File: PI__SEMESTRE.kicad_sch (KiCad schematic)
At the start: 36 parts, among them IC1 LMV358IDR, J1 CX90B-16P1, U1 AMS1117, U11 ESP32-S3-WROOM-1, U14 BME688, U9 GUVA-S12SD

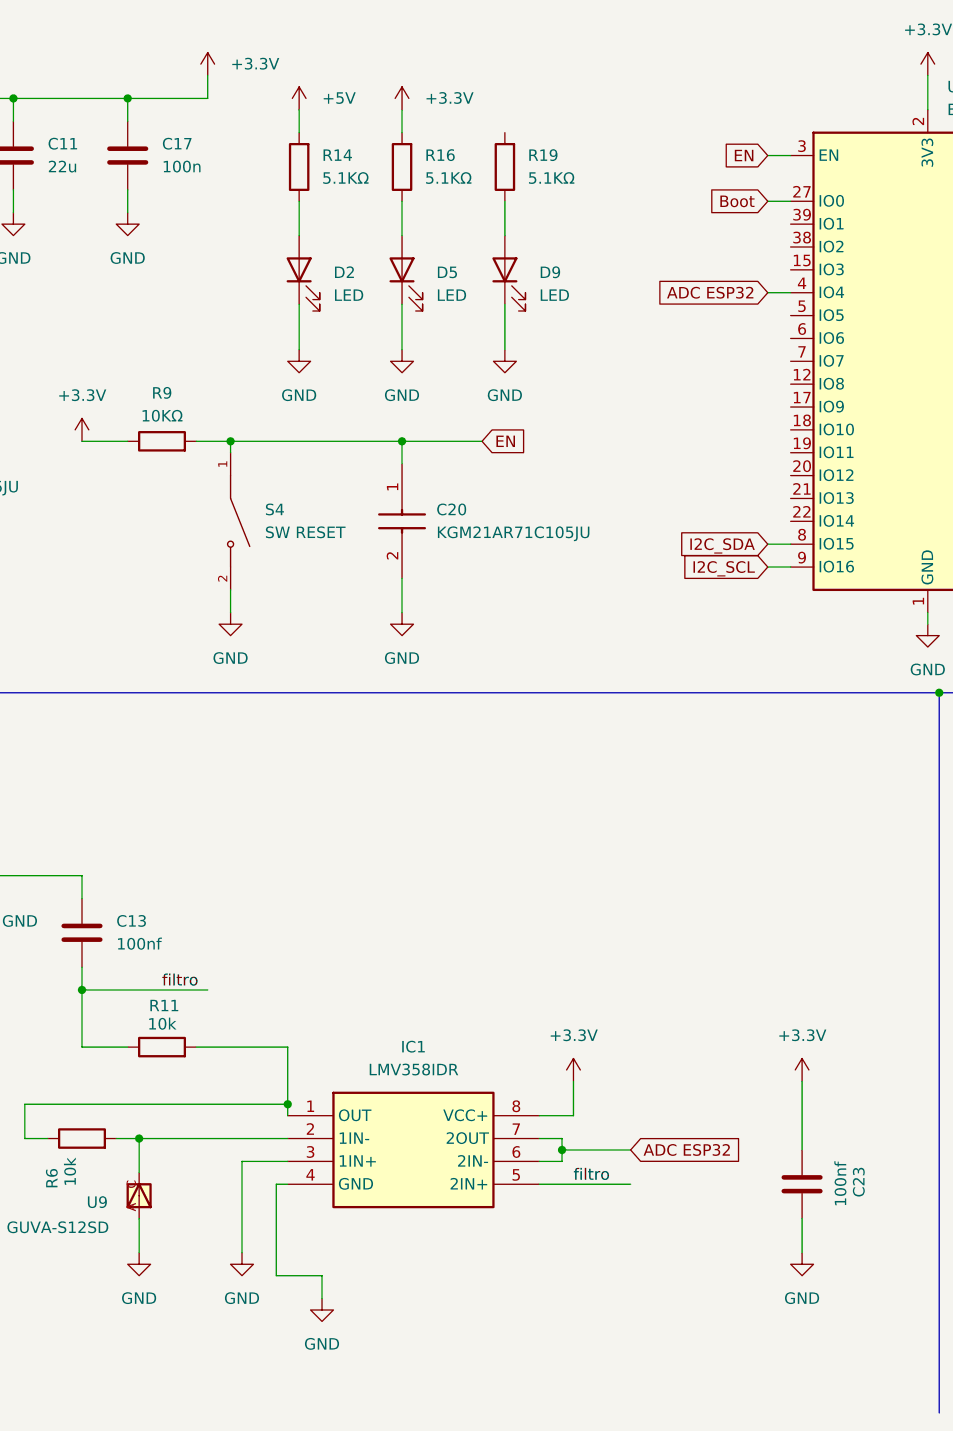
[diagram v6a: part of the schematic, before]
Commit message: se hacen los cambios de las pistas esquineras de (90 Grados) a curvas de (45 Grados) estos cambios solamente se le hicieron a las pistas azules, se le agrega la conexion del led faltante del (ESP) para nuestro KEEP ALIVE, se hace la conexion a algunas pistas faltantes que no se veian que habian por conectar, correciones de algunos GND sin conexion.
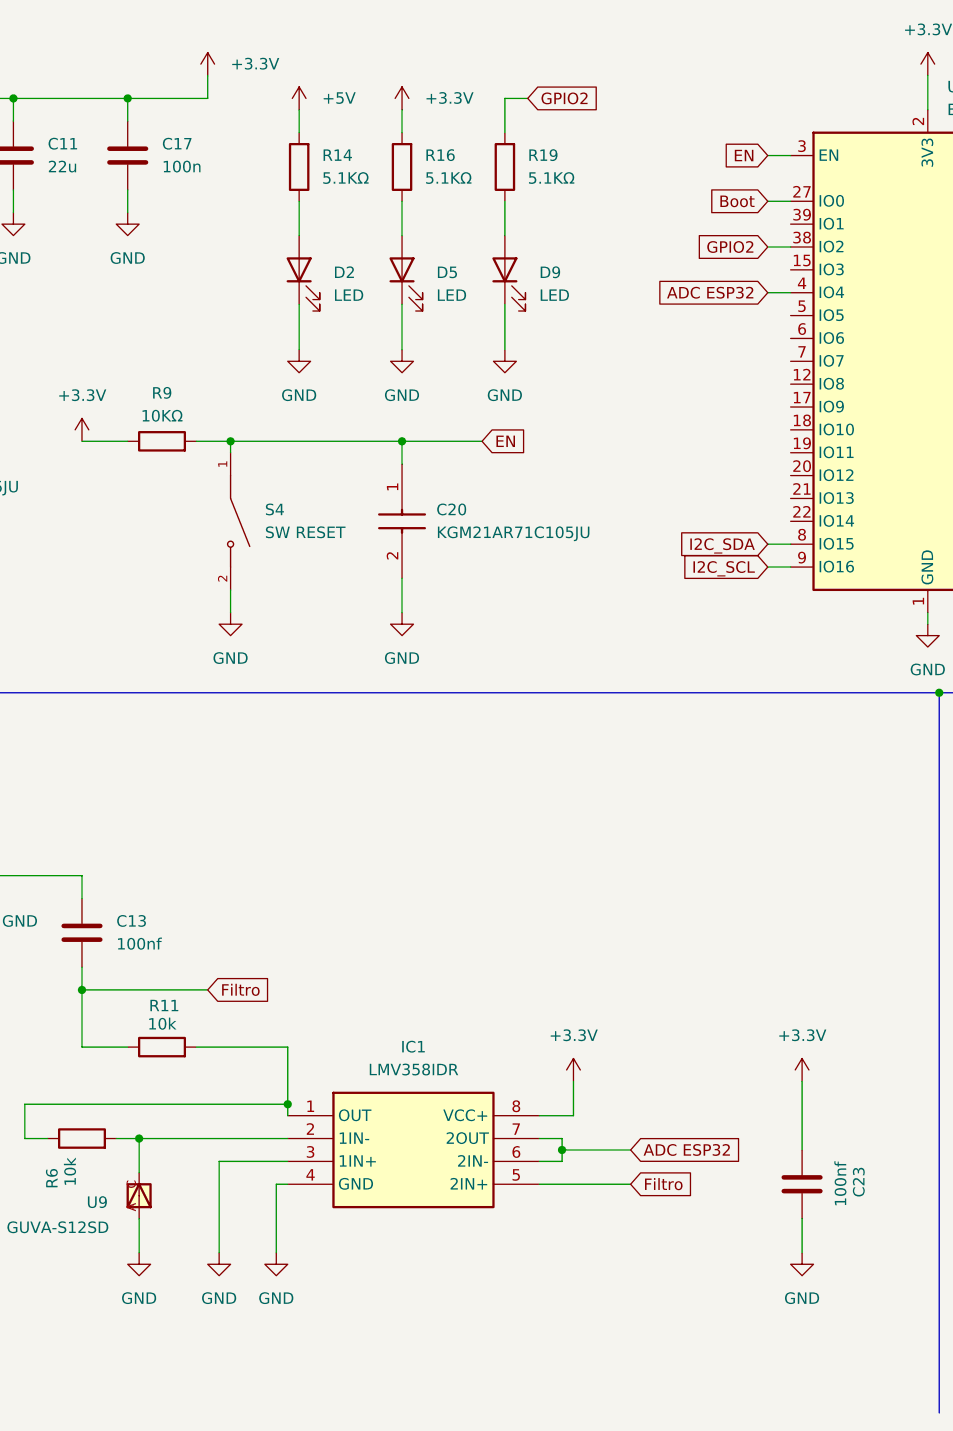
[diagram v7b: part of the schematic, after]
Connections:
- net GPIO2: now reaches R19.2
- net GPIO2: now also U11.38 (IO2)
- net filtro renamed Filtro
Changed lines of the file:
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@@
 	(wire
 		(pts
-			(xy 107.95 152.4) (xy 102.87 152.4)
-		)
-		(stroke
-			(width 0)
-			(type default)
-		)
-	)
-	(wire
-		(pts
 			(xy 232.41 130.81) (xy 234.95 130.81)
 		)
@@
 	(wire
 		(pts
-			(xy 99.06 139.7) (xy 99.06 149.86)
+			(xy 96.52 139.7) (xy 96.52 149.86)
 		)
 		(stroke
@@
 	(wire
 		(pts
+			(xy 128.27 21.59) (xy 130.81 21.59)
+		)
+		(stroke
+			(width 0)
+			(type default)
+		)
+	)
+	(wire
+		(pts
 			(xy 269.24 139.7) (xy 269.24 143.51)
 		)
@@
 	(wire
 		(pts
-			(xy 107.95 152.4) (xy 107.95 154.94)
+			(xy 73.66 24.13) (xy 73.66 21.59)
 		)
 		(stroke
@@
 	(wire
 		(pts
-			(xy 73.66 24.13) (xy 73.66 21.59)
+			(xy 224.79 33.02) (xy 224.79 35.56)
 		)
 		(stroke
@@
 	(wire
 		(pts
-			(xy 224.79 33.02) (xy 224.79 35.56)
+			(xy 128.27 25.4) (xy 128.27 21.59)
 		)
 		(stroke
@@
 	(wire
 		(pts
-			(xy 102.87 142.24) (xy 102.87 152.4)
+			(xy 102.87 142.24) (xy 102.87 149.86)
 		)
 		(stroke
@@
 	(wire
 		(pts
-			(xy 99.06 139.7) (xy 104.14 139.7)
+			(xy 96.52 139.7) (xy 104.14 139.7)
 		)
 		(stroke
@@
 	(wire
 		(pts
+			(xy 157.48 38.1) (xy 160.02 38.1)
+		)
+		(stroke
+			(width 0)
+			(type default)
+		)
+	)
+	(wire
+		(pts
 			(xy 93.98 127) (xy 104.14 127)
 		)
@@
 		)
 	)
-	(label "filtro"
-		(at 135.89 142.24 0)
-		(effects
-			(font
-				(size 1.27 1.27)
-			)
-			(justify left bottom)
-		)
-	)
-	(label "filtro"
-		(at 90.17 120.65 0)
-		(effects
-			(font
-				(size 1.27 1.27)
-			)
-			(justify left bottom)
-		)
-	)
 	(label "BME688"
 		(at 180.34 95.25 0)
@@
 		)
 	)
+	(global_label "Filtro"
+		(shape input)
+		(at 142.24 142.24 0)
+		(fields_autoplaced yes)
+		(effects
+			(font
+				(size 1.27 1.27)
+			)
+			(justify left)
+		)
+		(property "Intersheetrefs" "${INTERSHEET_REFS}"
+			(at 150.2447 142.24 0)
+			(hide yes)
+			(show_name no)
+			(do_not_autoplace no)
+			(effects
+				(font
+					(size 1.27 1.27)
+				)
+				(justify left)
+			)
+		)
+	)
 	(global_label "Boot"
 		(shape input)
@@
 		)
 	)
+	(global_label "Filtro"
+		(shape input)
+		(at 95.25 120.65 0)
+		(fields_autoplaced yes)
+		(effects
+			(font
+				(size 1.27 1.27)
+			)
+			(justify left)
+		)
+		(property "Intersheetrefs" "${INTERSHEET_REFS}"
+			(at 103.2547 120.65 0)
+			(hide yes)
+			(show_name no)
+			(do_not_autoplace no)
+			(effects
+				(font
+					(size 1.27 1.27)
+				)
+				(justify left)
+			)
+		)
+	)
 	(global_label "I2C_SDA"
 		(shape input)
@@
 		)
 	)
+	(global_label "GPIO2"
+		(shape input)
+		(at 130.81 21.59 0)
+		(fields_autoplaced yes)
+		(effects
+			(font
+				(size 1.27 1.27)
+			)
+			(justify left)
+		)
+		(property "Intersheetrefs" "${INTERSHEET_REFS}"
+			(at 139.48 21.59 0)
+			(hide yes)
+			(show_name no)
+			(do_not_autoplace no)
+			(effects
+				(font
+					(size 1.27 1.27)
+				)
+				(justify left)
+			)
+		)
+	)
 	(global_label "D-"
 		(shape input)
@@
 		)
 	)
+	(global_label "GPIO2"
+		(shape input)
+		(at 157.48 38.1 180)
+		(fields_autoplaced yes)
+		(effects
+			(font
+				(size 1.27 1.27)
+			)
+			(justify right)
+		)
+		(property "Intersheetrefs" "${INTERSHEET_REFS}"
+			(at 148.81 38.1 0)
+			(hide yes)
+			(show_name no)
+			(do_not_autoplace no)
+			(effects
+				(font
+					(size 1.27 1.27)
+				)
+				(justify right)
+			)
+		)
+	)
 	(symbol
 		(lib_id "power:GND")
@@
 	(symbol
 		(lib_id "power:GND")
-		(at 107.95 154.94 0)
+		(at 102.87 149.86 0)
 		(unit 1)
 		(body_style 1)
@@
 		(fields_autoplaced yes)
 		(property "Reference" "#PWR052"
-			(at 107.95 161.29 0)
+			(at 102.87 156.21 0)
 			(hide yes)
 			(show_name no)
@@
 		)
 		(property "Value" "GND"
-			(at 107.95 160.02 0)
+			(at 102.87 154.94 0)
 			(show_name no)
 			(do_not_autoplace no)
@@
 		)
 		(property "Footprint" ""
-			(at 107.95 154.94 0)
+			(at 102.87 149.86 0)
 			(hide yes)
 			(show_name no)
@@
 		)
 		(property "Datasheet" ""
-			(at 107.95 154.94 0)
+			(at 102.87 149.86 0)
 			(hide yes)
 			(show_name no)
@@
 		)
 		(property "Description" "Power symbol creates a global label with name \"GND\" , ground"
-			(at 107.95 154.94 0)
+			(at 102.87 149.86 0)
 			(hide yes)
 			(show_name no)
@@
 	(symbol
 		(lib_id "power:GND")
-		(at 99.06 149.86 0)
+		(at 96.52 149.86 0)
 		(unit 1)
 		(body_style 1)
@@
 		(fields_autoplaced yes)
 		(property "Reference" "#PWR045"
-			(at 99.06 156.21 0)
+			(at 96.52 156.21 0)
 			(hide yes)
 			(show_name no)
@@
 		)
 		(property "Value" "GND"
-			(at 99.06 154.94 0)
+			(at 96.52 154.94 0)
 			(show_name no)
 			(do_not_autoplace no)
@@
 		)
 		(property "Footprint" ""
-			(at 99.06 149.86 0)
+			(at 96.52 149.86 0)
 			(hide yes)
 			(show_name no)
@@
 		)
 		(property "Datasheet" ""
-			(at 99.06 149.86 0)
+			(at 96.52 149.86 0)
 			(hide yes)
 			(show_name no)
@@
 		)
 		(property "Description" "Power symbol creates a global label with name \"GND\" , ground"
-			(at 99.06 149.86 0)
+			(at 96.52 149.86 0)
 			(hide yes)
 			(show_name no)
